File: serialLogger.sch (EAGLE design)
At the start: 11 parts

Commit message: Initial v2 board.
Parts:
- removed A1: UNO, adafruit:ARDUINOUNO
- removed A2: (no value), SparkFun:M08LOCK
- removed INPUT: (no value), SparkFun:M02
- added C1, C2, C4: 10uF, _jc:C-USM0805
- added C10, C11, C7, C8, C9: 100nF, _jc:C-USM0805
- added C3: 1uF, _jc:C-USM0805
- added C5, C6: 22pF, _jc:C-USM0805
- added D4: 1N4148, _jc:DIODESOD-323F-A
- added J1: Ext Pwr, _jc:POWER-JACK
- added JP1: FTDI, SparkFun:M06LOCK
- added JP2: ICSP, _jc:AVR_SPI_PRG_62X3_LOCK
- added JP3: Pwr Select, SparkFun:M04LOCK
- added L1: 10uH, _jc:INDUCTORM0805
- added LOGO1, LOGO2: OSHW_LOGO_10MILX0200-NT, ohw-logo:OSHW_LOGO_10MILX0200-NT
- added R4: 10K, _jc:R-US_M0805
- added S3: RESET, _jc:10-XXOCT
- added U1: MCP1702, _jc:MCP1700SOT89
- added U2: MCP1700, _jc:MCP1700SOT23
- added U3: ATmega328P-AU, atmel:MEGA8-AI
- added U4: 74HC4050PW, 40xx:4050PW
- added X1: MICROSD, adafruit:MICROSD
- added Y1: 16MHz, _jc:CRYSTAL-2GNDTSX3225
- added Y2: (no value), _jc:CRYSTALABM2
- D1: value SD Activity -> Bfr Overrun (RED); device _jc:LED5MM -> _jc:LEDCHIPLED_1206
- D2: value Heartbeat -> SD Activity (YEL); device _jc:LED5MM -> _jc:LEDCHIPLED_1206
- D3: value Buffer Overrun -> Heartbeat (GRN); device _jc:LED5MM -> _jc:LEDCHIPLED_1206
- R2: value 1K -> 330
- S2: device switch-dil:219-04 -> _jc:OMRON-A6RS-102
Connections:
- removed net 3V: A2.2
- removed net 5V: A1.5V, A2.1
- removed net CLK: A1.D13, A2.4
- removed net CS: A1.D10, A2.7
- removed net DI: A1.D11, A2.6
- removed net DO: A1.D12, A2.5
- removed net N$11: A1.D5, D1.A
- removed net N$12: A1.D6, D2.A
- removed net N$13: A1.D7, D3.A
- removed net N$14: A1.D8, S1.S, S1.S1
- removed net N$5: A1.A3, S2.7
- removed net N$6: A1.A2, S2.8
- removed net N$7: D2.C, R2.2
- removed net N$8: D3.C, R3.2
- new net +3V3: C11.1, C4.1, U2.OUT, U4P.VDD, X1.VDD
- new net /RESET: C9.1, D4.A, JP2.RST, R4.1, S3.S, S3.S1, U3.PC6(/RESET)
- new net /SS: U3.PB2(SS/OC1B), U4A.I
- new net ADC0: S2.4, U3.PC0(ADC0)
- new net ADC1: S2.1, U3.PC1(ADC1)
- new net ADC2: S2.2, U3.PC2(ADC2)
- new net ADC3: S2.8, U3.PC3(ADC3)
- new net MISO: JP2.MISO, U3.PB4(MISO), X1.DATA_OUT
- new net MOSI: JP2.MOSI, U3.PB3(MOSI/OC2), U4B.I
- new net N$10: U4C.O, X1.SCLK
- new net N$15: U4A.O, X1.CS
- new net N$17: U4B.O, X1.DATA_IN
- new net N$18: C5.1, U3.PB6(XTAL1/TOSC1), Y1.1
- new net N$19: C6.1, U3.PB7(XTAL2/TOSC2), Y1.3
- new net N$20: C8.1, U3.AREF
- new net N$37: C7.1, L1.2, U3.AVCC
- new net PB0: R3.2, U3.PB0(ICP)
- new net PD5: S1.S, S1.S1, U3.PD5(T1)
- new net PD6: R1.2, U3.PD6(AIN0)
- new net PD7: R2.2, U3.PD7(AIN1)
- new net RST: C9.2, JP1.6
- new net RXD: JP1.4, U3.PD0(RXD)
- new net SCK: JP2.SCK, U3.PB5(SCK), U4C.I
- new net TXD: JP1.5, U3.PD1(TXD)
- new net VCC: C10.1, C2.1, C3.1, D4.K, JP1.3, JP2.VCC, JP3.4, L1.1, R4.2, U1.OUT, U2.IN, U3.VCC@1, U3.VCC@2
- new net VIN: J1.P$1, JP3.3
- net CD: now also U3.PB1(OC1A), X1.CARD_DETECT; no longer A1.D9, A2.8
- net GND: now also C1.2, C10.2, C11.2, C2.2, C3.2, C4.2, C5.2, C6.2, C7.2, C8.2, D1.C, D2.C, D3.C, J1.P$2, JP1.1, JP1.2, JP2.GND, JP3.1, S2.C, S3.P, S3.P1, U1.GND, U2.GND, U3.GND, U3.GND@1, U3.GND@2, U4D.I, U4E.I, U4F.I, U4P.VSS, X1.GND, X1.GND1, X1.VSS, Y1.2, Y1.4; no longer A1.GND, A1.GND1, A1.GND2, A2.3, INPUT.2, R1.1, R2.1, R3.1, S2.1, S2.2, S2.3, S2.4
- net N$1: now also D3.A, R3.1; no longer A1.D0, INPUT.1
- net N$2: now also D2.A, R2.1; no longer A1.A5, S2.5
- net N$3: now also D1.A, R1.1; no longer D1.C, R1.2
- net N$4: now also C1.1, JP3.2, U1.IN; no longer A1.A4, S2.6
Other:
- note added: "v2"
- note removed: "A2: Adafruit MicroSD card breakout board+ Product ID 254"
- note removed: "Uno"
- note removed: "v1"
- moved on the sheet: D1, D2, D3, R1, R2, R3, S1

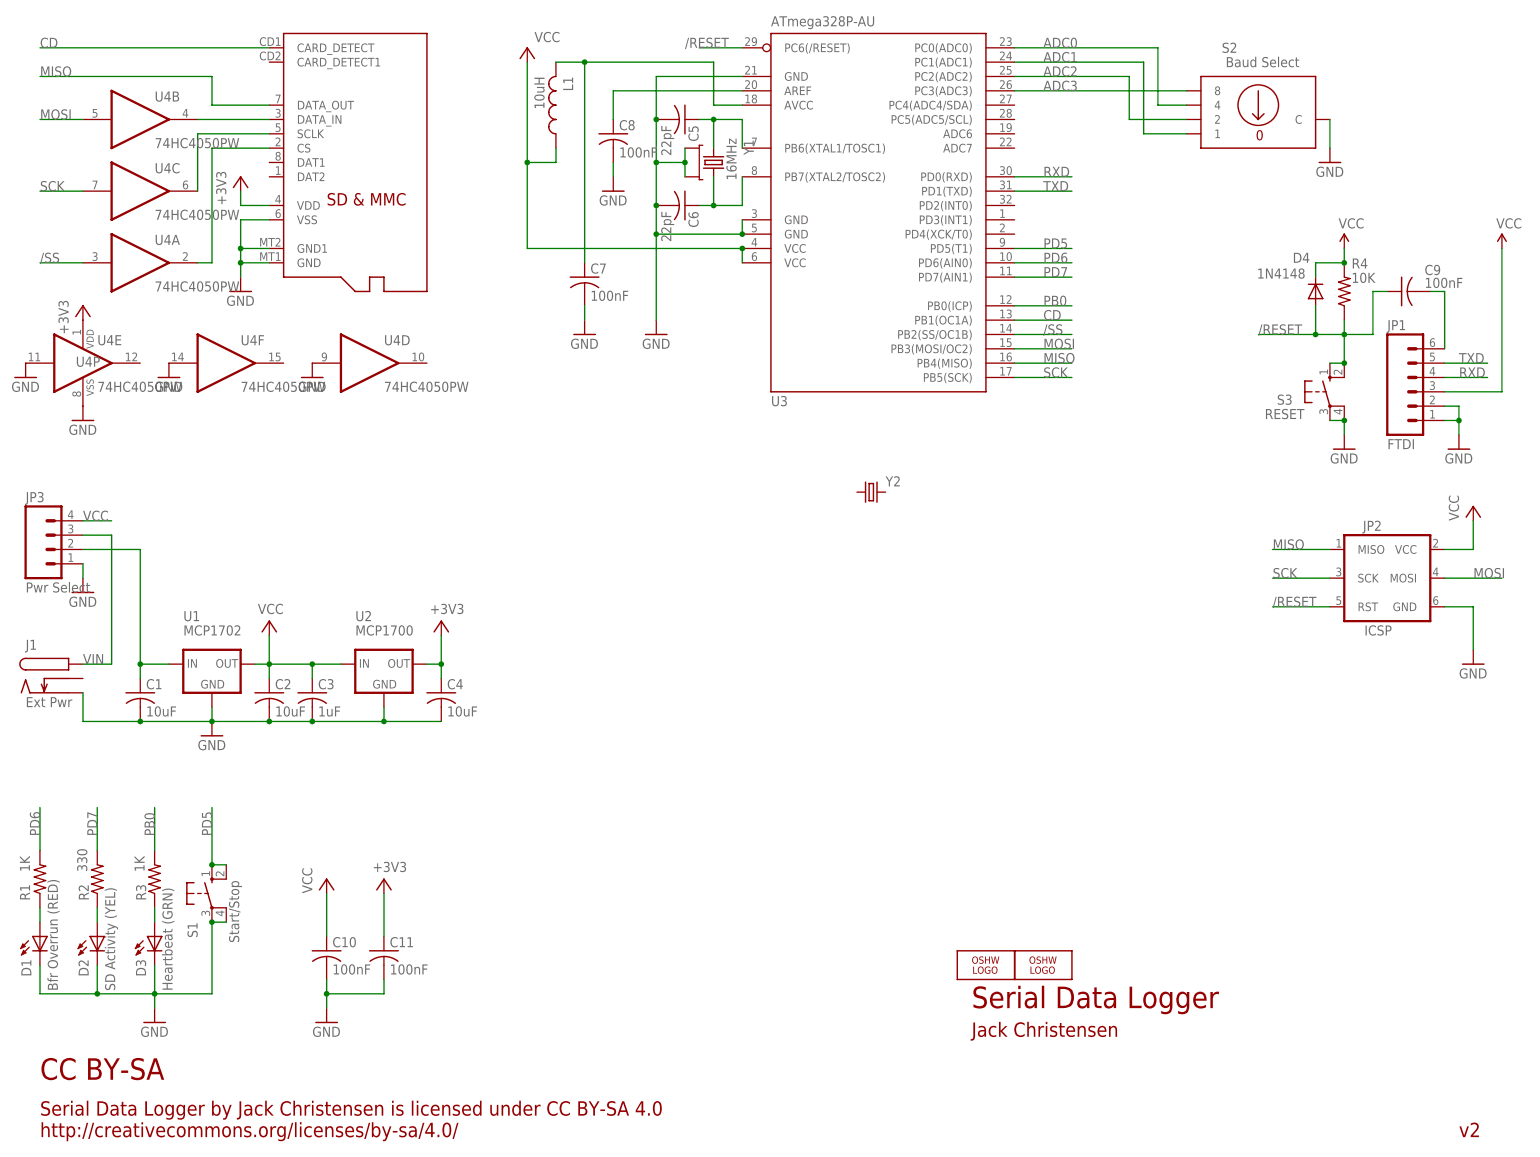
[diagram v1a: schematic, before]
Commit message: Change to Abracon xtal, refine board, add BOM spreadsheet.
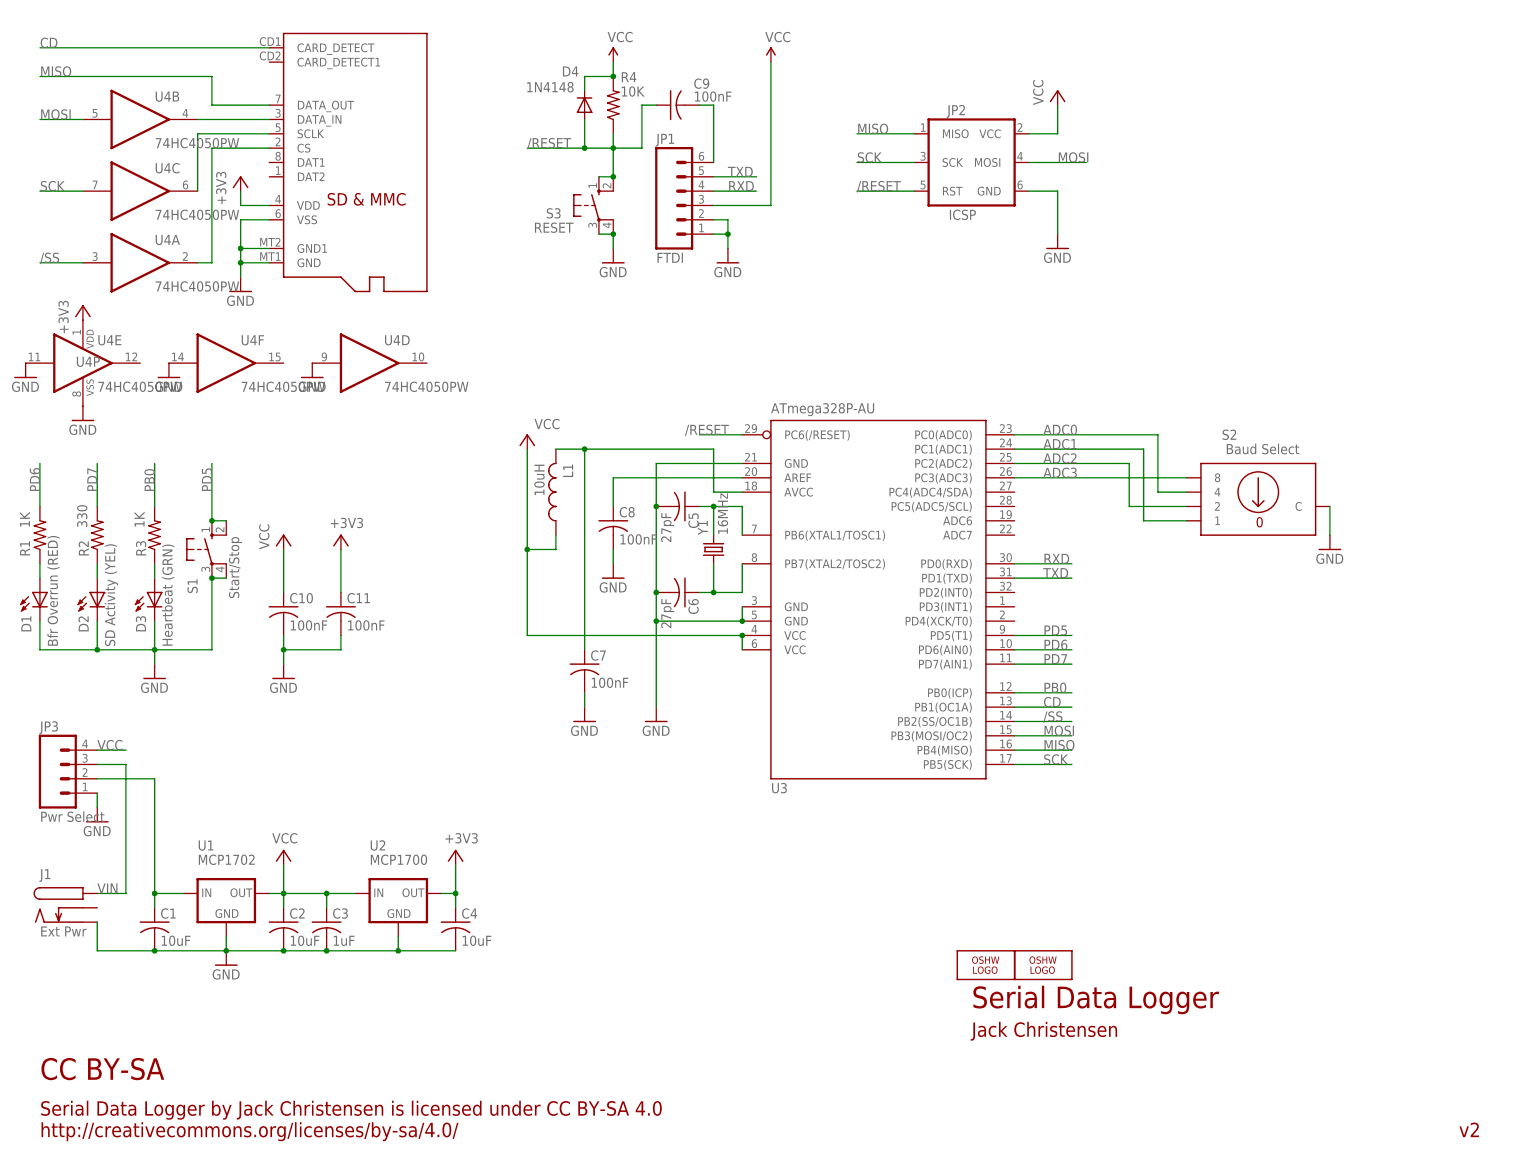
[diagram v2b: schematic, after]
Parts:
- removed Y2: (no value), _jc:CRYSTALABM2
- C5, C6: value 22pF -> 27pF
- Y1: device _jc:CRYSTAL-2GNDTSX3225 -> _jc:CRYSTALABM2
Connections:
- net GND: no longer Y1.2, Y1.4
- net N$18: now also Y1.2; no longer Y1.1
- net N$19: now also Y1.1; no longer Y1.3
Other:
- moved on the sheet: C1, C10, C11, C2, C3, C4, C5, C6, C7, C8, C9, D1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

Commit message: Final v2 board
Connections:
- net ADC3 renamed N$8
- removed net ADC0: S2.4, U3.PC0(ADC0)
- removed net ADC1: S2.1, U3.PC1(ADC1)
- removed net ADC2: S2.2, U3.PC2(ADC2)
- new net N$5: S2.1, U3.PC0(ADC0)
- new net N$6: S2.2, U3.PC1(ADC1)
- new net N$7: S2.4, U3.PC2(ADC2)
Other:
- moved on the sheet: S2
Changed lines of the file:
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@@
 <attribute name="VALUE" x="51.308" y="59.69" size="1.778" layer="96"/>
 </instance>
-<instance part="S2" gate="G$1" x="226.06" y="121.92" smashed="yes">
-<attribute name="NAME" x="220.98" y="132.08" size="1.778" layer="95" align="center"/>
-<attribute name="VALUE" x="226.822" y="129.54" size="1.778" layer="96" align="center"/>
+<instance part="S2" gate="G$1" x="213.36" y="127" smashed="yes" rot="MR180">
+<attribute name="NAME" x="208.28" y="116.84" size="1.778" layer="95" rot="MR180" align="center"/>
+<attribute name="VALUE" x="214.122" y="119.38" size="1.778" layer="96" rot="MR180" align="center"/>
 </instance>
-<instance part="GND4" gate="1" x="238.76" y="111.76"/>
+<instance part="GND4" gate="1" x="226.06" y="116.84"/>
 <instance part="+3V1" gate="G$1" x="63.5" y="114.3" smashed="yes">
 <attribute name="VALUE" x="61.468" y="115.57" size="1.778" layer="96"/>
@@
 <pinref part="S2" gate="G$1" pin="C"/>
 <pinref part="GND4" gate="1" pin="GND"/>
-<wire x1="238.76" y1="119.38" x2="238.76" y2="114.3" width="0.1524" layer="91"/>
+<wire x1="226.06" y1="129.54" x2="226.06" y2="119.38" width="0.1524" layer="91"/>
 </segment>
 <segment>
@@
 </segment>
 </net>
-<net name="ADC3" class="0">
-<segment>
-<pinref part="U3" gate="G$1" pin="PC3(ADC3)"/>
-<wire x1="182.88" y1="124.46" x2="213.36" y2="124.46" width="0.1524" layer="91"/>
-<label x="187.96" y="124.46" size="1.778" layer="95"/>
-<pinref part="S2" gate="G$1" pin="8"/>
-</segment>
-</net>
-<net name="ADC2" class="0">
-<segment>
-<pinref part="U3" gate="G$1" pin="PC2(ADC2)"/>
-<label x="187.96" y="127" size="1.778" layer="95"/>
-<pinref part="S2" gate="G$1" pin="2"/>
-<wire x1="213.36" y1="119.38" x2="203.2" y2="119.38" width="0.1524" layer="91"/>
-<wire x1="203.2" y1="119.38" x2="203.2" y2="127" width="0.1524" layer="91"/>
-<wire x1="203.2" y1="127" x2="182.88" y2="127" width="0.1524" layer="91"/>
-</segment>
-</net>
-<net name="ADC1" class="0">
-<segment>
-<pinref part="U3" gate="G$1" pin="PC1(ADC1)"/>
-<wire x1="182.88" y1="129.54" x2="205.74" y2="129.54" width="0.1524" layer="91"/>
-<label x="187.96" y="129.54" size="1.778" layer="95"/>
-<pinref part="S2" gate="G$1" pin="1"/>
-<wire x1="213.36" y1="116.84" x2="205.74" y2="116.84" width="0.1524" layer="91"/>
-<wire x1="205.74" y1="116.84" x2="205.74" y2="129.54" width="0.1524" layer="91"/>
-</segment>
-</net>
-<net name="ADC0" class="0">
-<segment>
-<pinref part="U3" gate="G$1" pin="PC0(ADC0)"/>
-<wire x1="182.88" y1="132.08" x2="208.28" y2="132.08" width="0.1524" layer="91"/>
-<label x="187.96" y="132.08" size="1.778" layer="95"/>
-<pinref part="S2" gate="G$1" pin="4"/>
-<wire x1="213.36" y1="121.92" x2="208.28" y2="121.92" width="0.1524" layer="91"/>
-<wire x1="208.28" y1="121.92" x2="208.28" y2="132.08" width="0.1524" layer="91"/>
-</segment>
-</net>
 <net name="/SS" class="0">
 <segment>
@@
 </segment>
 </net>
+<net name="N$5" class="0">
+<segment>
+<pinref part="S2" gate="G$1" pin="1"/>
+<pinref part="U3" gate="G$1" pin="PC0(ADC0)"/>
+<wire x1="200.66" y1="132.08" x2="182.88" y2="132.08" width="0.1524" layer="91"/>
+</segment>
+</net>
+<net name="N$6" class="0">
+<segment>
+<pinref part="S2" gate="G$1" pin="2"/>
+<pinref part="U3" gate="G$1" pin="PC1(ADC1)"/>
+<wire x1="200.66" y1="129.54" x2="182.88" y2="129.54" width="0.1524" layer="91"/>
+</segment>
+</net>
+<net name="N$7" class="0">
+<segment>
+<pinref part="S2" gate="G$1" pin="4"/>
+<pinref part="U3" gate="G$1" pin="PC2(ADC2)"/>
+<wire x1="200.66" y1="127" x2="182.88" y2="127" width="0.1524" layer="91"/>
+</segment>
+</net>
+<net name="N$8" class="0">
+<segment>
+<pinref part="S2" gate="G$1" pin="8"/>
+<pinref part="U3" gate="G$1" pin="PC3(ADC3)"/>
+<wire x1="200.66" y1="124.46" x2="182.88" y2="124.46" width="0.1524" layer="91"/>
+</segment>
+</net>
